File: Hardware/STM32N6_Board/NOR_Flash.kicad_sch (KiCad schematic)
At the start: 16 parts, among them U7 MX25LM51245GXDI00, U8 SPX5205-ADJ

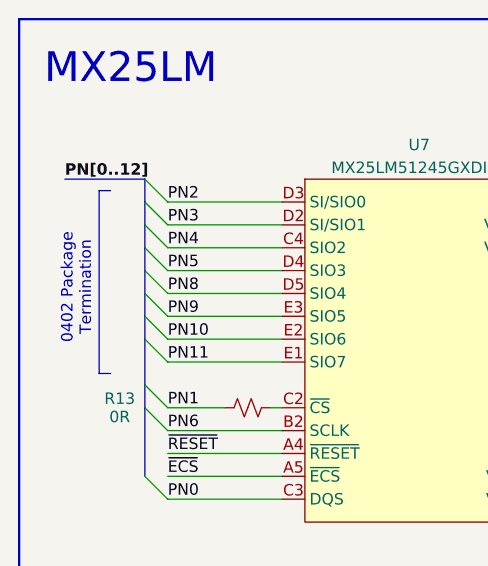
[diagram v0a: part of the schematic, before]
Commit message: Updated the schematic with latest changes
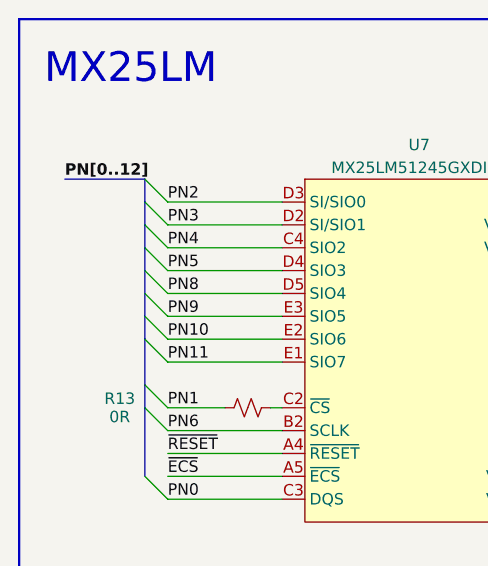
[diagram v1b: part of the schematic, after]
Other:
- note removed: "0402 Package Termination"
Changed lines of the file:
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@@
-		)
-	)
-	(text "0402 Package\nTermination"
-		(exclude_from_sim no)
-		(at 41.148 45.212 90)
-		(effects
-			(font
-				(size 1.27 1.27)
-			)
-			(justify bottom)
 		)
 	)
@@
 		)
 	)
-	(polyline
-		(pts
-			(xy 41.91 34.29) (xy 41.91 54.61)
-		)
-		(stroke
-			(width 0)
-			(type default)
-		)
-	)
 	(bus
 		(pts
@@
 		)
 	)
-	(polyline
-		(pts
-			(xy 41.91 54.61) (xy 43.18 54.61)
-		)
-		(stroke
-			(width 0)
-			(type default)
-		)
-	)
 	(wire
 		(pts
@@
 		)
 		(stroke
-			(width 0)
-			(type default)
-		)
-	)
-	(polyline
-		(pts
-			(xy 43.18 34.29) (xy 41.91 34.29)
-		)
-		(stroke

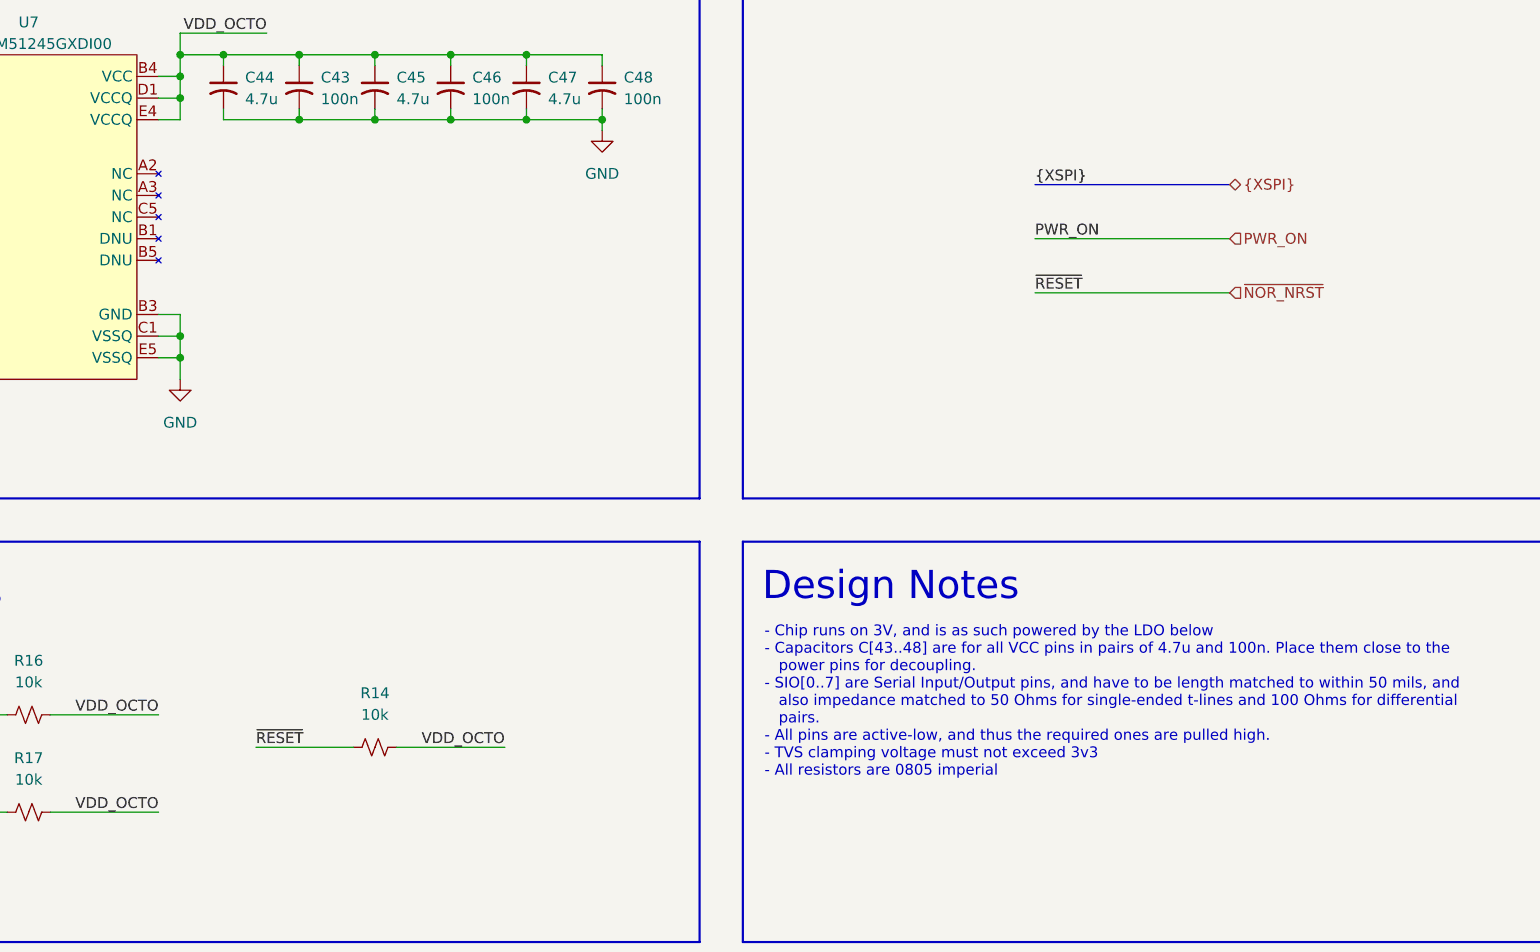
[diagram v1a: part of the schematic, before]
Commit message: Fanned out and routed the MX25LM. Much easier.
- The NOR flash chip is now fanned out, routed, and bypass caps are
  placed.
- Still need bypass caps on the IS42S
- I also changed the SDRAM clock a little, to avoid a small loop.
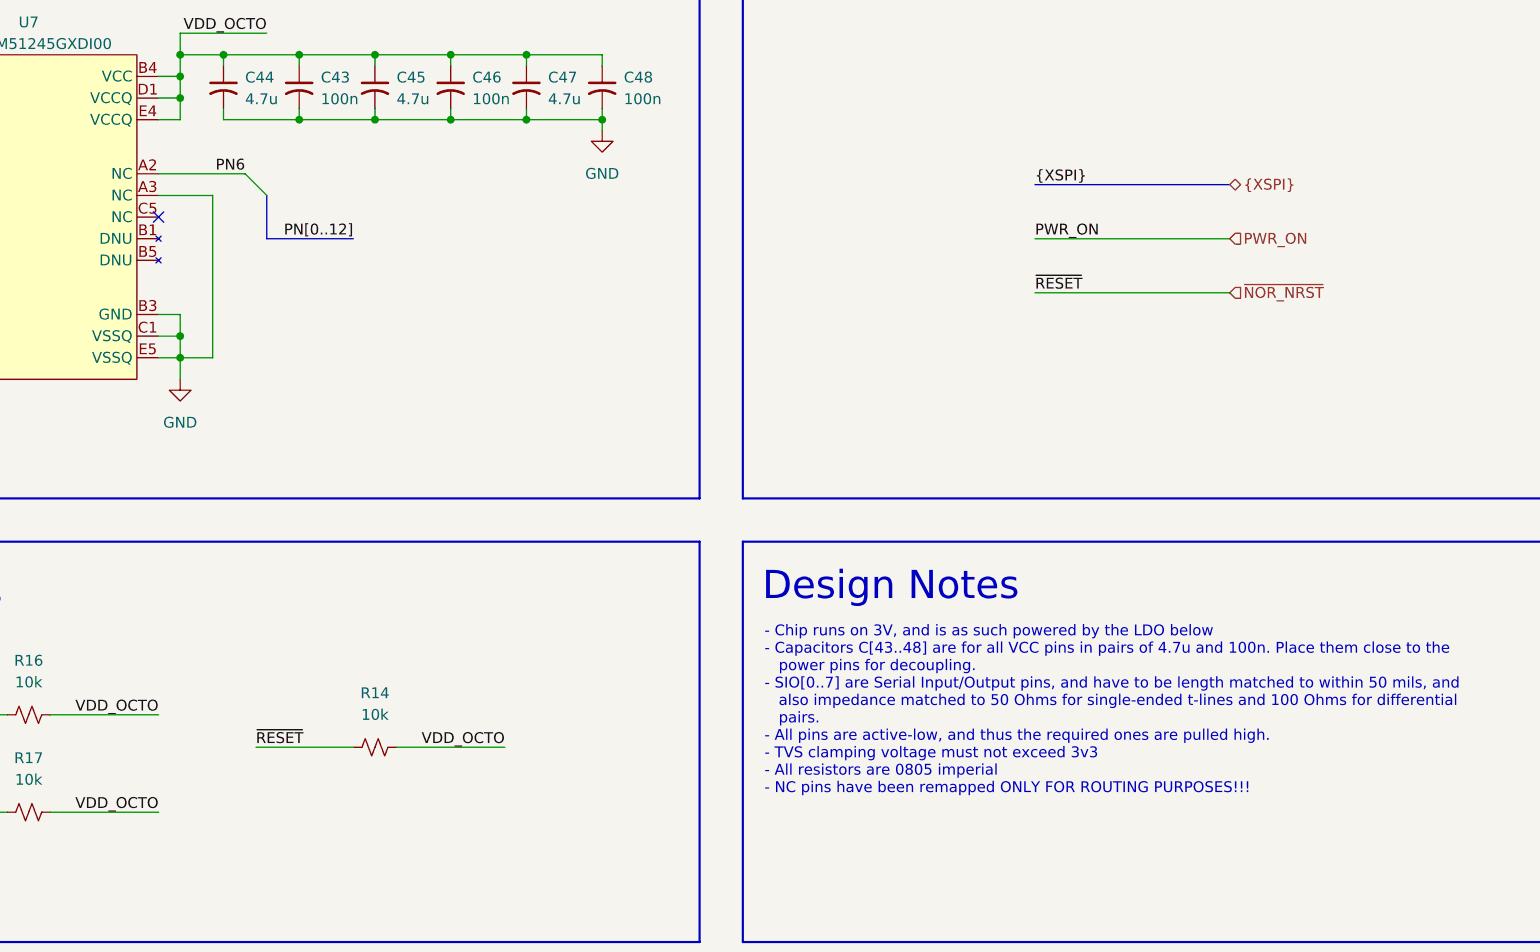
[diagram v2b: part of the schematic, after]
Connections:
- net GND: now also U7.A3 (NC)
- net PN6: now also U7.A2 (NC)
- no-connect marks 0 -> 1
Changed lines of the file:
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@@
 		)
 	)
-	(text "- Chip runs on 3V, and is as such powered by the LDO below\n- Capacitors C[43..48] are for all VCC pins in pairs of 4.7u and 100n. Place them close to the\n   power pins for decoupling.\n- SIO[0..7] are Serial Input/Output pins, and have to be length matched to within 50 mils, and \n   also impedance matched to 50 Ohms for single-ended t-lines and 100 Ohms for differential\n   pairs.\n- All pins are active-low, and thus the required ones are pulled high.\n- TVS clamping voltage must not exceed 3v3\n- All resistors are 0805 imperial"
+	(text "- Chip runs on 3V, and is as such powered by the LDO below\n- Capacitors C[43..48] are for all VCC pins in pairs of 4.7u and 100n. Place them close to the\n   power pins for decoupling.\n- SIO[0..7] are Serial Input/Output pins, and have to be length matched to within 50 mils, and \n   also impedance matched to 50 Ohms for single-ended t-lines and 100 Ohms for differential\n   pairs.\n- All pins are active-low, and thus the required ones are pulled high.\n- TVS clamping voltage must not exceed 3v3\n- All resistors are 0805 imperial\n- NC pins have been remapped ONLY FOR ROUTING PURPOSES!!!"
 		(exclude_from_sim no)
 		(at 163.83 100.076 0)
@@
 		(color 0 0 0 0)
 	)
+	(no_connect
+		(at 92.71 52.07)
+	)
 	(bus_entry
 		(at 49.53 43.18)
@@
 	)
 	(bus_entry
+		(at 105.41 49.53)
+		(size -2.54 -2.54)
+		(stroke
+			(width 0)
+			(type default)
+		)
+	)
+	(bus_entry
 		(at 49.53 53.34)
 		(size -2.54 -2.54)
@@
 	(wire
 		(pts
+			(xy 99.06 68.58) (xy 95.25 68.58)
+		)
+		(stroke
+			(width 0)
+			(type default)
+		)
+	)
+	(wire
+		(pts
 			(xy 95.25 33.02) (xy 95.25 30.48)
 		)
@@
 	(wire
 		(pts
+			(xy 92.71 46.99) (xy 102.87 46.99)
+		)
+		(stroke
+			(width 0)
+			(type default)
+		)
+	)
+	(wire
+		(pts
 			(xy 81.28 162.56) (xy 81.28 165.1)
 		)
@@
 	(wire
 		(pts
+			(xy 99.06 49.53) (xy 99.06 68.58)
+		)
+		(stroke
+			(width 0)
+			(type default)
+		)
+	)
+	(wire
+		(pts
 			(xy 95.25 68.58) (xy 95.25 71.12)
 		)
@@
 		)
 	)
+	(bus
+		(pts
+			(xy 105.41 49.53) (xy 105.41 54.61)
+		)
+		(stroke
+			(width 0)
+			(type default)
+		)
+	)
+	(wire
+		(pts
+			(xy 92.71 49.53) (xy 99.06 49.53)
+		)
+		(stroke
+			(width 0)
+			(type default)
+		)
+	)
 	(wire
 		(pts
@@
 		(pts
 			(xy 135.89 33.02) (xy 135.89 34.29)
+		)
+		(stroke
+			(width 0)
+			(type default)
+		)
+	)
+	(bus
+		(pts
+			(xy 105.41 54.61) (xy 115.57 54.61)
 		)
 		(stroke
@@
 		)
 	)
+	(label "PN[0..12]"
+		(at 115.57 54.61 180)
+		(effects
+			(font
+				(size 1.27 1.27)
+				(thickness 0.1588)
+			)
+			(justify right bottom)
+		)
+	)
 	(label "VDD_OCTO"
 		(at 116.84 165.1 180)
 		(effects
 			(font
+				(size 1.27 1.27)
+			)
+			(justify right bottom)
+		)
+	)
+	(label "PN6"
+		(at 102.87 46.99 180)
+		(effects
+			(font
